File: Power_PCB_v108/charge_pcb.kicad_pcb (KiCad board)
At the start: 2 copper layers, 128.1 x 64 mm, 73 parts, among them J1 Mow3, J10 Mot_Left, J11 DC/DC1, J12 DC/DC2, J2 Main_PCB1, J3 Mow2, J4 Battery, J5 Main_PCB2, J6 Power Switch, J7 Mow1, J8 Mot_Right, J9 Start, Q1 BC547C, Q2 IRF9540N, Q3 BC547C, Q4 IRF9540N, U1 INA226, U2 INA226, U3 INA226, U4 INA226, U5 INA226, U6 INA226

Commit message: Routing and change some Places
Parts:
- moved C1 26.2 mm to (198.1, 65.0), turned to -90 degrees
- moved R4 11.9 mm to (122.2, 81.0), turned to -90 degrees
- moved R2 11.8 mm to (95.5, 84.3)
- moved kibuzzard-6311B784 11.1 mm to (138.9, 75.9), turned to 90 degrees
- moved kibuzzard-6311B799 8.36 mm to (136.4, 75.9), turned to 90 degrees
- moved Q1 6.37 mm to (109.9, 84.8)
- moved R3 6.14 mm to (113.3, 81.3)
- moved R1 4.85 mm to (103.1, 81.3)
- moved Q4 3.87 mm to (179.9, 76.7), turned to -90 degrees
- moved Q3 3.18 mm to (187.4, 71.5)
- moved Q2 2.95 mm to (118.3, 87.6)
- moved D4 2.55 mm to (141.7, 85.7)
- moved U3 0.57 mm to (135.1, 72.4), turned to 0 degrees
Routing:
- net +3V3: track 0.00 -> 143.9 mm, vias 0 -> 1
- net SCL0: track 0.00 -> 139.9 mm
- net SDA0: track 0.00 -> 127.7 mm
- net pinBatterySwitch: track 0.00 -> 113.4 mm
- net GND: track 0.00 -> 92.6 mm
- net SCL1: track 0.00 -> 75.3 mm
- net SDA1: track 0.00 -> 73.1 mm
- net pinChargeEnable: track 0.00 -> 20.9 mm
- net Net-(J9-Pad1): track 19.3 -> 34.3 mm
- net V_Bat: track 243.5 -> 255.7 mm
- net Net-(Q3-Pad2): track 0.00 -> 11.3 mm
- net Net-(D3-Pad2): track 20.1 -> 10.1 mm
- net Net-(J4-Pad1): track 39.3 -> 30.5 mm
- net Net-(Q2-Pad2): track 24.9 -> 33.6 mm
- net Net-(Q1-Pad2): track 0.00 -> 7.51 mm
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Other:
- board text added: "PowerPCB V1.08"
- board text removed: "PowerPCB V1.07"

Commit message: Change Diode
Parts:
- added JP1: Jumper Charge, Connector_PinHeader_2.54mm:PinHeader_1x02_P2.54mm_Vertical, F.Cu at (123.2, 55.4)
- moved D3 10.2 mm to (121.2, 75.4), turned to 180 degrees
- moved D5 9.91 mm to (159.5, 85.9), turned to 180 degrees
- moved R5 4.06 mm to (190.0, 79.0)
- moved R6 4.06 mm to (190.0, 83.1)
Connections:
- D3 pad 1: Net-(D1-Pad1) -> Net-(D3-Pad1)
- D3 pad 2: Net-(D3-Pad2) -> Net-(D1-Pad1)
- D5 pad 1: Net-(D4-Pad1) -> Net-(D5-Pad1)
- D5 pad 2: Net-(D5-Pad2) -> Net-(D4-Pad1)
- Q2 pad 3: Net-(D3-Pad2) -> Net-(D3-Pad1)
- Q4 pad 3: Net-(D5-Pad2) -> Net-(D5-Pad1)
- R4 pad 1: Net-(D3-Pad2) -> Net-(D3-Pad1)
- R7 pad 1: Net-(D5-Pad2) -> Net-(D5-Pad1)
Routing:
- net Net-(D5-Pad2): track 24.8 -> 0.00 mm
- net Net-(D5-Pad1): track 0.00 -> 24.8 mm
- net GND: track 92.6 -> 81.8 mm
- net Net-(D3-Pad2): track 10.1 -> 0.00 mm
- net Net-(D3-Pad1): track 0.00 -> 10.1 mm
- net Net-(Q3-Pad2): track 11.3 -> 14.7 mm

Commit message: Routing and Gerber Files
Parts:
- moved R7 29.5 mm to (192.0, 79.0)
- moved JP1 15.5 mm to (125.7, 70.6), turned to 180 degrees
- moved D5 13.2 mm to (172.7, 85.9)
- moved D1 12.1 mm to (115.8, 80.8)
- moved J9 9.15 mm to (186.2, 66.5)
- moved R3 9.00 mm to (104.6, 83.8)
- moved kibuzzard-630F6FC9 8.89 mm to (187.2, 62.5)
- moved kibuzzard-630F7110 8.38 mm to (161.8, 62.5)
- moved kibuzzard-630F70A7 7.87 mm to (173.7, 62.5)
- moved J6 7.80 mm to (171.4, 67.8)
- moved R5 7.40 mm to (192.0, 86.1)
- moved J4 7.37 mm to (158.2, 67.8)
- moved F2 7.37 mm to (167.6, 78.2)
- moved Q1 6.99 mm to (116.4, 87.3), turned to 180 degrees
- moved Q3 6.84 mm to (193.7, 74.0)
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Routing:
- net Net-(JP1-Pad2): track 30.5 -> 53.8 mm
- net GND: track 81.8 -> 97.7 mm
- net Net-(D3-Pad1): track 10.1 -> 23.5 mm
- net Net-(D4-Pad1): track 16.9 -> 28.3 mm
- net SDA0: track 127.7 -> 137.7 mm
- net Net-(J9-Pad1): track 34.3 -> 25.0 mm
- net pinChargeEnable: track 20.9 -> 13.9 mm
- net +3V3: track 143.9 -> 137.5 mm
- net pinBatterySwitch: track 113.4 -> 108.9 mm
- net Net-(D2-Pad2): track 4.49 -> 8.34 mm
- net Net-(Q3-Pad2): track 14.7 -> 10.9 mm
- net SCL0: track 139.9 -> 136.2 mm, vias 0 -> 1
- net Net-(Q1-Pad2): track 7.51 -> 10.6 mm
- net Net-(D5-Pad1): track 24.8 -> 22.3 mm
- net Net-(Q1-Pad1): track 13.9 -> 11.4 mm
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
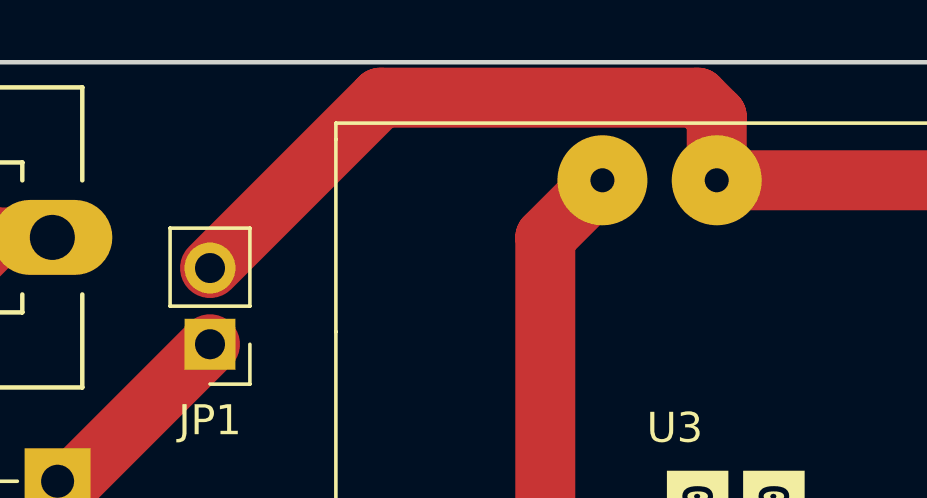
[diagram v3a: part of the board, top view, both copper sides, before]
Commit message: Connection from jumper changed
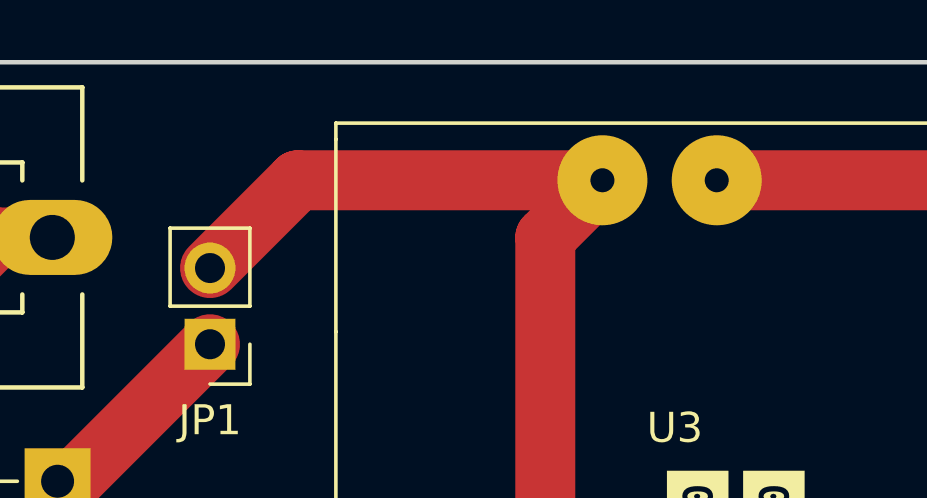
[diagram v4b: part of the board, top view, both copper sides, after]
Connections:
- J4 pad 1: Net-(JP1-Pad2) -> Net-(J4-Pad1)
- J6 pad 1: Net-(JP1-Pad2) -> Net-(J4-Pad1)
- JP1 pad 2: Net-(JP1-Pad2) -> Net-(Q2-Pad2)
- U3 pad 10: Net-(JP1-Pad2) -> Net-(J4-Pad1)
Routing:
- net Net-(JP1-Pad2): track 53.8 -> 0.00 mm
- net Net-(J4-Pad1): track 0.00 -> 32.2 mm
- net Net-(Q2-Pad2): track 33.1 -> 47.4 mm
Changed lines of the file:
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@@
   (net 43 "Net-(Q2-Pad2)")
   (net 44 "Net-(D5-Pad1)")
-  (net 45 "Net-(JP1-Pad2)")
+  (net 45 "Net-(J4-Pad1)")
   (footprint "Zimprich:Anschlussklemme_2P_RM5,08" (layer "F.Cu")
     (at 91.44 73.406 -90)
@@
     (fp_line (start -2.41 2.55) (end 7.49 2.55) (layer "F.Fab") (width 0.1))
     (pad "1" thru_hole rect locked (at 0 0) (size 3 3) (drill 1.52) (layers *.Cu *.Mask)
-      (net 45 "Net-(JP1-Pad2)") (pintype "passive"))
+      (net 45 "Net-(J4-Pad1)") (pintype "passive"))
     (pad "2" thru_hole circle locked (at 5.08 0) (size 3 3) (drill 1.52) (layers *.Cu *.Mask)
       (net 1 "GND") (pintype "passive"))
@@
     (fp_line (start 7.54 3.75) (end 7.54 -3.75) (layer "F.Fab") (width 0.1))
     (pad "1" thru_hole rect locked (at 0 0) (size 3 3) (drill 1.52) (layers *.Cu *.Mask)
-      (net 45 "Net-(JP1-Pad2)") (pintype "passive"))
+      (net 45 "Net-(J4-Pad1)") (pintype "passive"))
     (pad "2" thru_hole circle locked (at 5.08 0) (size 3 3) (drill 1.52) (layers *.Cu *.Mask)
       (net 2 "Net-(F2-Pad1)") (pintype "passive"))
@@
       (net 43 "Net-(Q2-Pad2)") (pinfunction "IN1+") (pintype "input"))
     (pad "10" thru_hole oval locked (at 1.905 -8.255) (size 3 3) (drill 0.8) (layers *.Cu *.Mask)
-      (net 45 "Net-(JP1-Pad2)") (pinfunction "IN1-") (pintype "input"))
+      (net 45 "Net-(J4-Pad1)") (pinfunction "IN1-") (pintype "input"))
   )
   (footprint "Current_sense:INA226" (layer "F.Cu")
@@
       (net 42 "Net-(D3-Pad1)") (pinfunction "1") (pintype "passive"))
     (pad "2" thru_hole oval locked (at 0 2.54 180) (size 1.7 1.7) (drill 1) (layers *.Cu *.Mask)
-      (net 45 "Net-(JP1-Pad2)") (pinfunction "2") (pintype "passive"))
+      (net 43 "Net-(Q2-Pad2)") (pinfunction "2") (pintype "passive"))
     (model "${KISYS3DMOD}/Connector_PinHeader_2.54mm.3dshapes/PinHeader_1x02_P2.54mm_Vertical.wrl"
       (offset (xyz 0 0 0))
@@
   (segment (start 136.906 78.74) (end 136.906 81.026) (width 2) (layer "F.Cu") (net 43))
   (segment (start 129.705 78.74) (end 136.906 78.74) (width 2) (layer "F.Cu") (net 43))
+  (segment (start 128.656 65.151) (end 125.73 68.077) (width 2) (layer "F.Cu") (net 43))
+  (segment (start 138.811 65.151) (end 128.656 65.151) (width 2) (layer "F.Cu") (net 43))
   (segment (start 122.865 84.582) (end 123.863 84.582) (width 2) (layer "F.Cu") (net 43))
   (segment (start 136.906 67.056) (end 136.906 78.74) (width 2) (layer "F.Cu") (net 43))
@@
   (segment (start 185.237 79.502) (end 191.716 79.502) (width 2) (layer "F.Cu") (net 44))
   (segment (start 192.024 79.194) (end 192.024 78.994) (width 0.254) (layer "F.Cu") (net 44))
-  (segment (start 142.621 63.0297) (end 141.989 62.3975) (width 2) (layer "F.Cu") (net 45))
   (segment (start 142.621 65.151) (end 155.575 65.151) (width 2) (layer "F.Cu") (net 45))
-  (segment (start 141.989 62.3975) (end 131.41 62.3975) (width 2) (layer "F.Cu") (net 45))
-  (segment (start 142.621 65.151) (end 142.621 63.0297) (width 2) (layer "F.Cu") (net 45))
   (segment (start 168.696 65.0645) (end 171.45 67.818) (width 2) (layer "F.Cu") (net 45))
-  (segment (start 131.41 62.3975) (end 125.73 68.077) (width 2) (layer "F.Cu") (net 45))
   (segment (start 160.996 65.0645) (end 168.696 65.0645) (width 2) (layer "F.Cu") (net 45))
   (segment (start 155.575 65.151) (end 158.242 67.818) (width 2) (layer "F.Cu") (net 45))

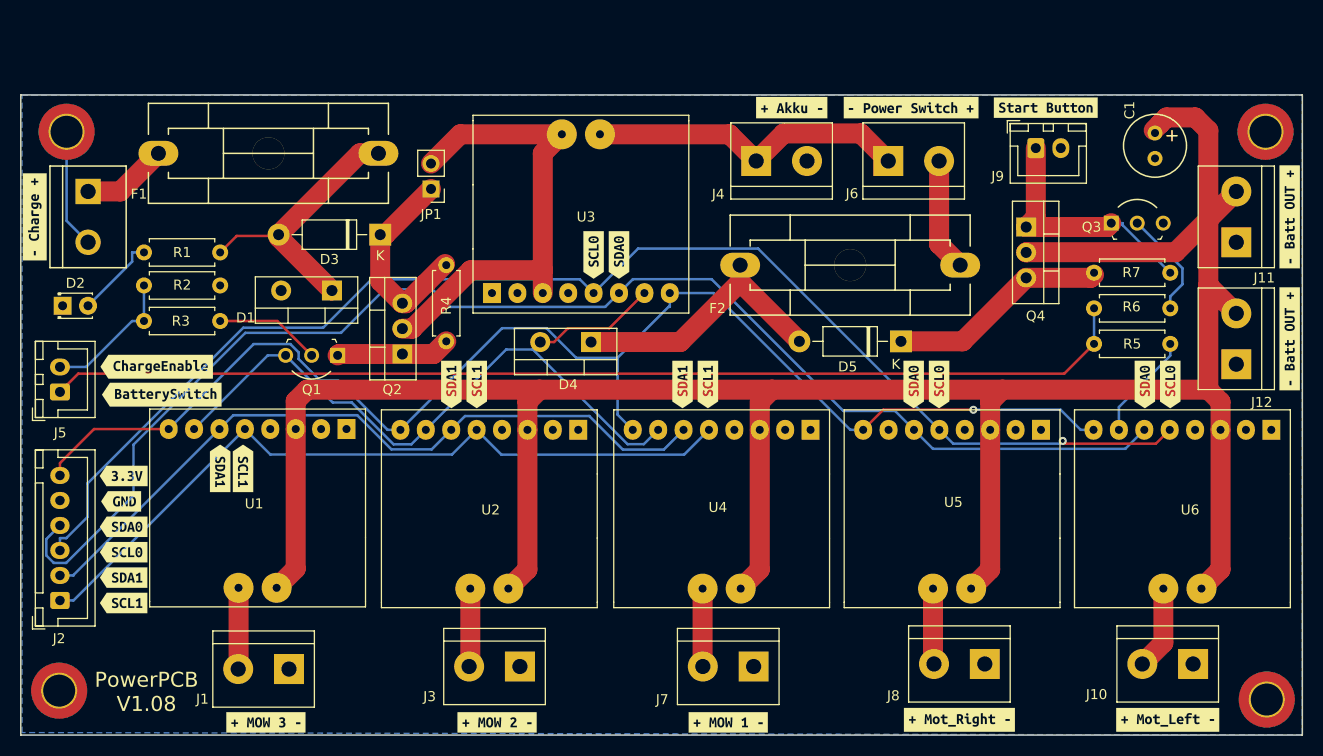
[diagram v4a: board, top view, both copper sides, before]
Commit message: Add MBR1045
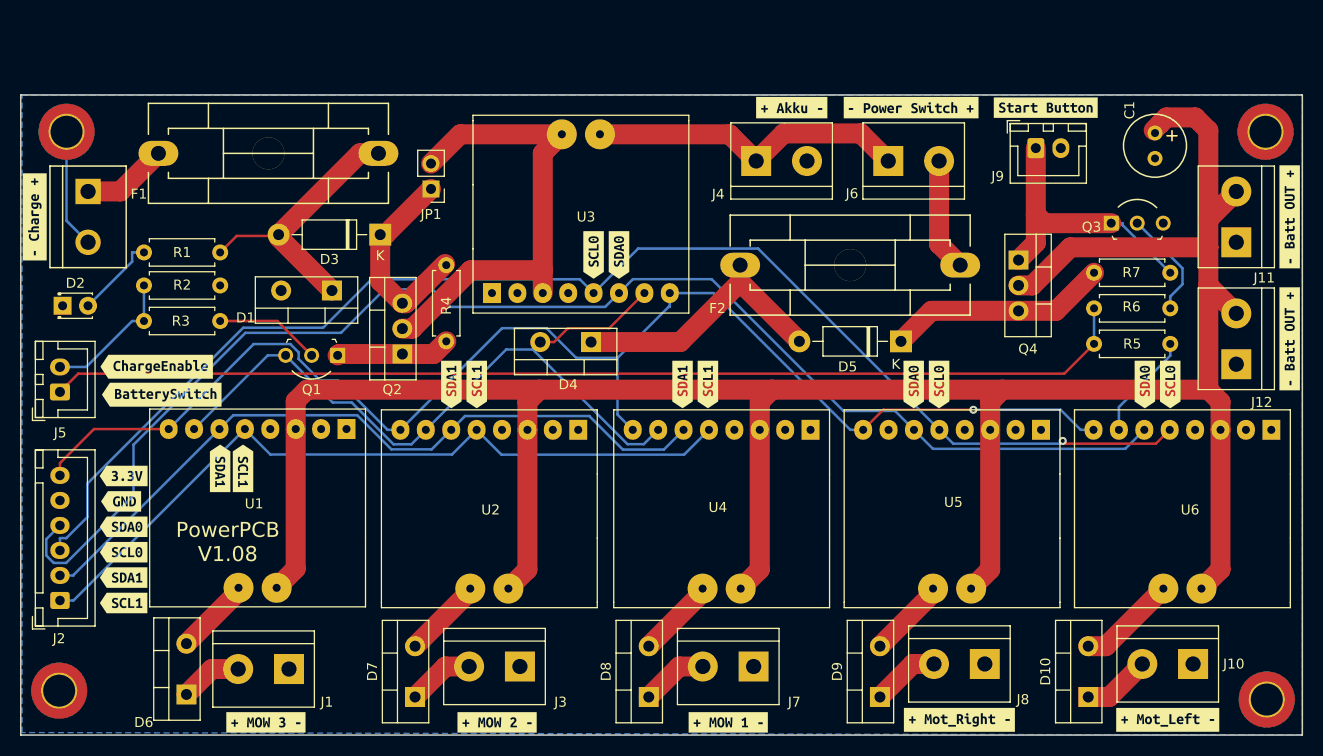
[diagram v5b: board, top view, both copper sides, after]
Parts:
- added D10: MBR1045, Package_TO_SOT_THT:TO-220-2_Vertical, F.Cu at (191.4, 121.4)
- added D6: MBR1045, Package_TO_SOT_THT:TO-220-2_Vertical, F.Cu at (101.3, 121.2)
- added D7: MBR1045, Package_TO_SOT_THT:TO-220-2_Vertical, F.Cu at (124.1, 121.4)
- added D8: MBR1045, Package_TO_SOT_THT:TO-220-2_Vertical, F.Cu at (147.5, 121.4)
- added D9: MBR1045, Package_TO_SOT_THT:TO-220-2_Vertical, F.Cu at (170.6, 121.4)
- moved Q4 3.39 mm to (184.5, 77.7)
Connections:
- U1 pad 10: Net-(J1-Pad2) -> Net-(U1-Pad10)
- U2 pad 10: Net-(J3-Pad2) -> Net-(U2-Pad10)
- U4 pad 10: Net-(J7-Pad2) -> Net-(U4-Pad10)
- U5 pad 10: Net-(J8-Pad2) -> Net-(U5-Pad10)
- U6 pad 10: Net-(J10-Pad2) -> Net-(U6-Pad10)
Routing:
- net Net-(U6-Pad10): track 0.00 -> 9.89 mm
- net Net-(U2-Pad10): track 0.00 -> 8.04 mm
- net Net-(U4-Pad10): track 0.00 -> 7.99 mm
- net Net-(U5-Pad10): track 0.00 -> 7.96 mm
- net Net-(U1-Pad10): track 0.00 -> 7.74 mm
- net Net-(J9-Pad1): track 25.0 -> 27.9 mm
- net Net-(J1-Pad2): track 8.14 -> 6.23 mm
- net Net-(J10-Pad2): track 8.41 -> 6.77 mm
- net Net-(J3-Pad2): track 7.84 -> 6.67 mm
- net Net-(J7-Pad2): track 7.80 -> 6.67 mm
- net V_Bat: track 257.0 -> 258.0 mm
- net Net-(J8-Pad2): track 7.58 -> 6.77 mm
